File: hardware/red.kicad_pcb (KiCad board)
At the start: 6 copper layers, 40 x 40 mm, 190 parts, among them J1 MICROSDCARD, J2 USB-A, J3 MICRO_HDMI, J4 USB-MINI-B-SMD, J5 STACK-UP-LOW, J6 STACK-DOWN, J7 STACK-UP-LOW, J8 STACK-DOWN, P1 Camera/EXT, Q1 2N7002, Q2 2N7002, Q3 2N7002, SW1 RESET_SW, U1 H5TQ4G63AFR, U2 AXP152, U3 RT9701XB, U4 82400152, U5 TPD4S010DQA, U6 TPD4S010DQA, U7 TPD4S010DQA, U8 82400152, U9 NX3008PBKS, X1 24MHz

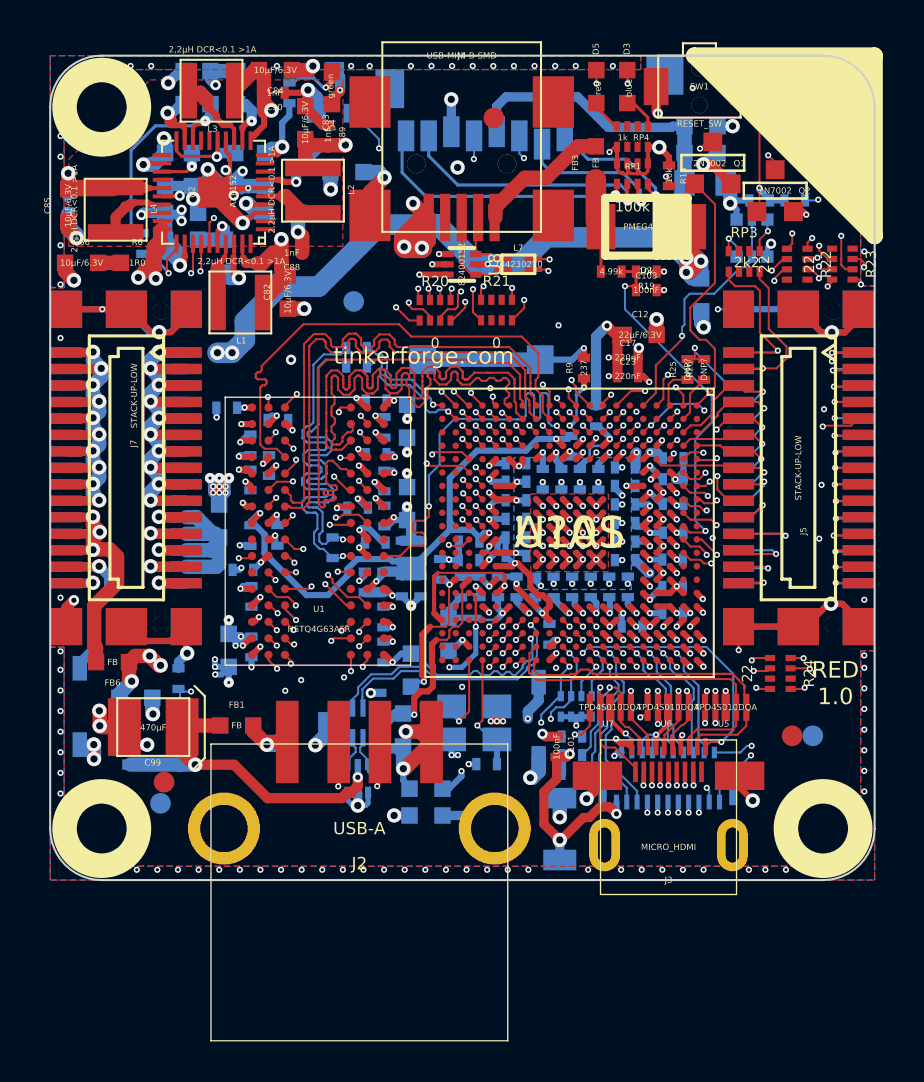
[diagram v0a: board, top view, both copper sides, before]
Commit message: ordered hardware version changed assignment of resistor networks for sdcard signals
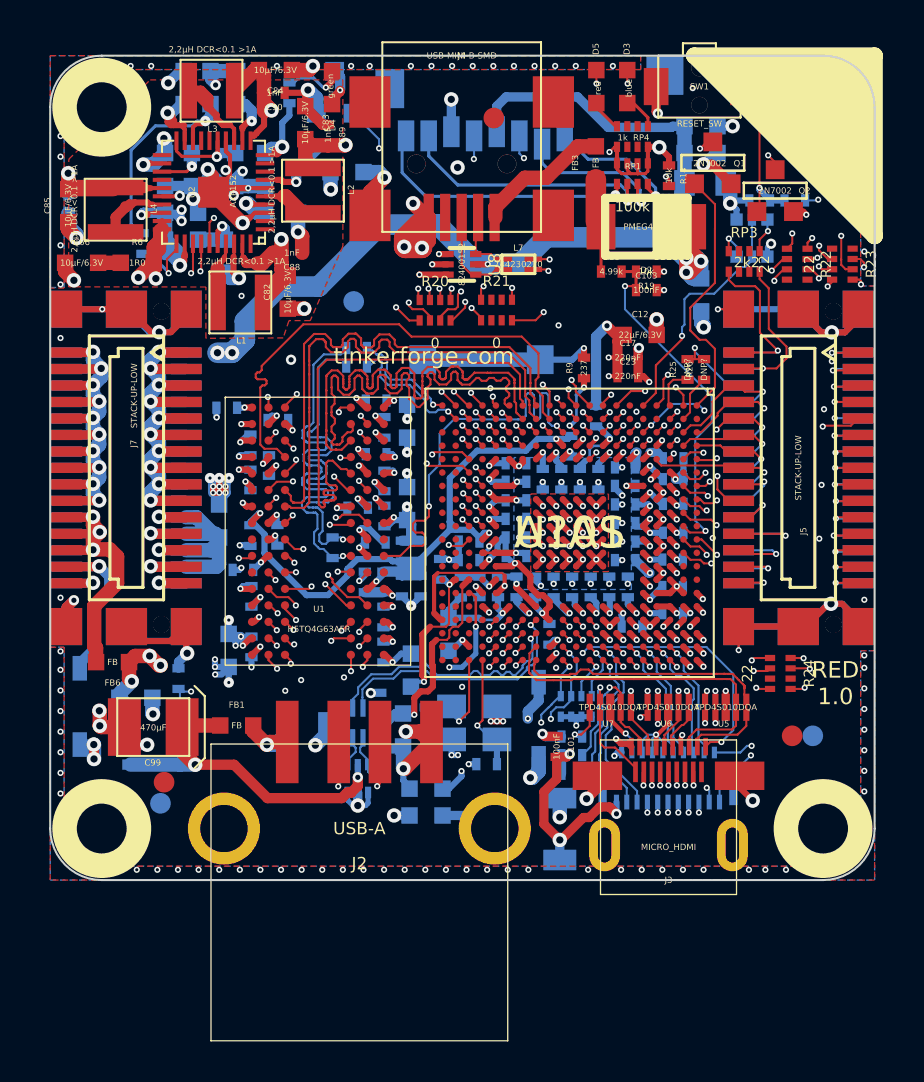
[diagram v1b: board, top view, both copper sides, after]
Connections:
- R20 pad 3: N-00000229 -> N-00000246
- R20 pad 4: N-00000244 -> N-00000243
- R20 pad 5: SDCARD_CMD -> SDCARD_D2
- R20 pad 6: SDCARD_CLK -> SDCARD_D3
- R21 pad 1: N-00000246 -> N-00000244
- R21 pad 4: N-00000243 -> N-00000231
- R21 pad 5: SDCARD_D2 -> SDCARD_CLK
- R21 pad 8: SDCARD_D3 -> SDCARD_CMD
- U?A1 pad K18: N-00000229 -> N-00000231
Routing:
- net N-00000229: track 26.9 -> 0.00 mm, vias 2 -> 0
- net N-00000231: track 0.00 -> 22.1 mm, vias 0 -> 2
- net GND: track 807.3 -> 811.1 mm, vias 313 -> 314
- net SDCARD_D2: track 16.1 -> 19.1 mm
- net N-00000243: track 22.3 -> 25.2 mm
- net SDCARD_D3: track 17.8 -> 19.8 mm
- net SDCARD_CMD: track 17.3 -> 19.1 mm
- net N-00000246: track 27.0 -> 27.9 mm
- net N-00000244: track 24.4 -> 23.5 mm

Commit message: add current hardware version
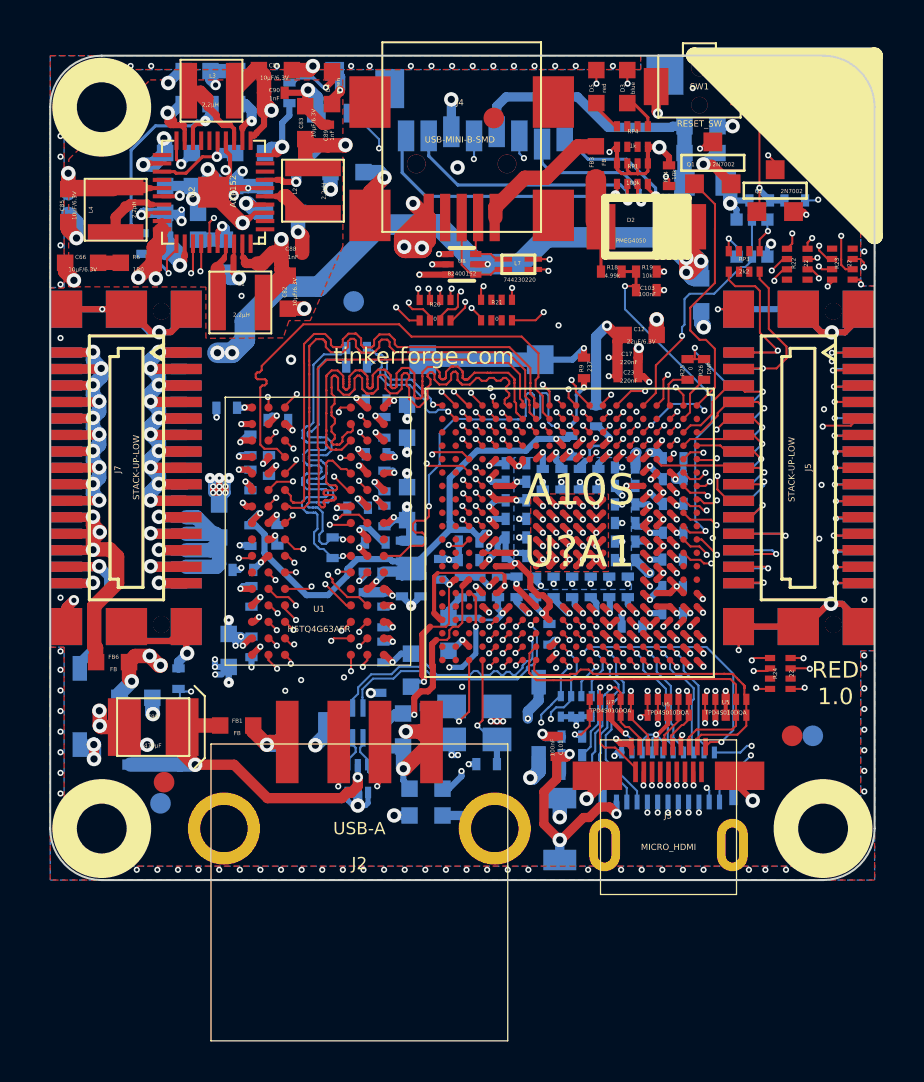
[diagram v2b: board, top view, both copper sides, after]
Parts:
- C100: value TBD -> 100nF
- C15, C3: value TBDpF -> 9pF
- C95: value NA -> DNP
- L1, L2, L3, L4: value 2,2µH DCR<0.1 >1A -> 2,2µH
- R25: value DNP? -> 0
- R26: value DNP? -> DNP
- moved C63 2.10 mm to (134.2, 80.5)
- moved C64 2.10 mm to (136.3, 80.5)
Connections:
- C63 pad 1: N-000007 (its old number) -> N-000008
- C64 pad 1: N-000008 -> N-000009
- U2 pad 15: N-000007 (its old number) -> N-000009
- U2 pad 20: N-000007 (its old number) -> N-000008
- U2 pad 23: N-000008 -> N-000009
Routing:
- net N-000007 (its old number): track 5.10 -> 0.00 mm, vias 1 -> 0
- net N-000009: track 0.00 -> 4.78 mm, vias 0 -> 1
- net LDO0_OUT: track 55.1 -> 53.3 mm

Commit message: * reset button is now used as power button * change reset circuitry:   * stack reset is now connected to interrupt capable GPIO   * RESET_N signal is now used only for internal reset circuitry * fix USB ESD protection ciruitry bug * add inverter for STACK-SER2-RTS signal * UART3_CTS connected to GND * add missing tf logo * change position of different components and labels for easier production
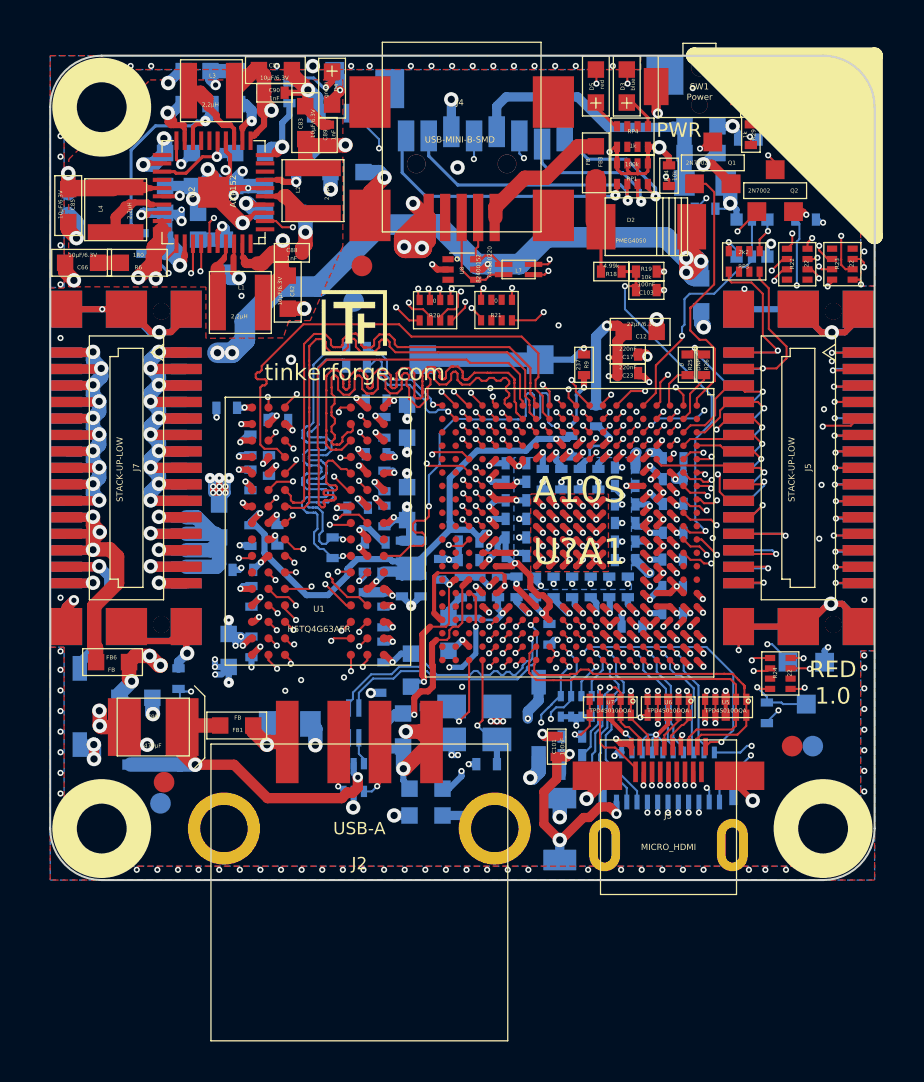
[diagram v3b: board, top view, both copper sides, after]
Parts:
- added C30: 100pF, tinkerforge:0402, B.Cu at (161.2, 79.0)
- added G***: Logo_31x31, logo:Logo_31x31, F.Cu at (140.5, 86.3)
- added Q4: 2N7002, SOT23GDS, B.Cu at (164.0, 105.4)
- added R29: 1k, tinkerforge:0402, F.Cu at (161.3, 78.8)
- added R30: 1k, 0402, B.Cu at (162.1, 106.8)
- C1, C10, C101, C103, C11, C13, C15, C16, C17, C18, C19, C2, C20, C21, C22, C23, C24, C27, C28, C29, C3, C31, C32, C34, C35, C36, C37, C38, C39, C4, C40, C41, C42, C43, C44, C45, C46, C47, C49, C5, C50, C51, C52, C53, C54, C55, C57, C59, C6, C65, C67, C68, C69, C7, C70, C71, C72, C73, C79, C8, C80, C81, C86, C87, C88, C89, C9, C90, C91, C93, C94, C95, R1, R10, R11, R12, R13, R14, R15, R16, R17, R18, R19, R2, R25, R26, R27, R3, R4, R5, R7, R8, R9: footprint 0402 -> tinkerforge:0402
- C100, L5: footprint 0805 -> tinkerforge:0805
- C102, C12, C14, C25, C26, C33, C48, C56, C58, C60, C61, C62, C63, C64, C66, C74, C75, C76, C77, C78, C82, C83, C84, C85, C92, C96, C97, C98, FB1, FB2, FB3, FB4, FB5, FB6, R6: footprint 0603 -> tinkerforge:0603
- C99: footprint 3528-21 -> tinkerforge:3528-21
- D1, D6: footprint SOD-123 -> tinkerforge:SOD-123
- D2: footprint SOD-128 -> tinkerforge:SOD-128
- D3, D4, D5: footprint D0603 -> tinkerforge:D0603
- F1: footprint 1206 -> tinkerforge:1206
- J1: footprint MicroSD_TF001A -> tinkerforge:MicroSD_TF001A
- J2: footprint USB-A-SMT-8231 -> tinkerforge:USB-A-SMT-8231
- J3: footprint MICRO-HDMI-D -> tinkerforge:MICRO-HDMI-D
- J4: footprint USB-MINI-B-SMD -> tinkerforge:USB-MINI-B-SMD
- J5, J7: footprint BTB08-ACS-TOP -> tinkerforge:BTB08-ACS-TOP
- J6, J8: footprint BTB08-ACS-BTM -> tinkerforge:BTB08-ACS-BTM
- L1, L2, L3, L4: footprint NRH3015 -> tinkerforge:NRH3015
- L6, L7: footprint WE-CNSW-0603 -> tinkerforge:WE-CNSW-0603
- P1: footprint 502078-2110-C -> tinkerforge:502078-2110-C
- Q1, Q2, Q3: footprint SOT23GDS -> tinkerforge:SOT23GDS
- R20, R21, R22, R23, R24, RP1, RP2, RP3, RP4: footprint 741X083 -> tinkerforge:741X083
- R28: value 1k -> 100; footprint 0402 -> tinkerforge:0402
- SW1: value RESET_SW -> Power; footprint TACT-SWITCH -> tinkerforge:TACT-SWITCH
- U1: footprint FBGA96 -> tinkerforge:FBGA96
- U2: footprint QFN40_5X5 -> tinkerforge:QFN40_5X5
- U3: footprint SOT23-5 -> tinkerforge:SOT23-5
- U4, U8: footprint SOT563 -> tinkerforge:SOT563
- U5, U6, U7: footprint TPD4S010DQA -> tinkerforge:TPD4S010DQA
- U9: footprint SOT363 -> tinkerforge:SOT363
- U?A1: footprint TFBGA336 -> tinkerforge:TFBGA336
- X1: footprint CRYSTAL_3225 -> tinkerforge:CRYSTAL_3225
- moved Fiducial_Mark 9.61 mm to (142.4, 85.1)
- moved VAL 5.91 mm to (139.1, 88.1)
- moved R3 2.68 mm to (159.1, 82.3), turned to 180 degrees
- moved R28 1.06 mm to (164.0, 82.9)
- moved C100 0.88 mm to (138.9, 107.3)
- moved Fiducial_Mark 0.50 mm to (163.3, 108.4)
- moved Fiducial_Mark 0.50 mm to (164.3, 108.4)
- moved L7 0.25 mm to (150.1, 85.3)
- moved U8 0.25 mm to (147.3, 85.3)
- moved R25 0.23 mm to (158.2, 89.9)
- moved R26 0.23 mm to (159.1, 89.9)
- moved U4 0.21 mm to (142.1, 110.0)
- moved L6 0.20 mm to (142.1, 107.3)
- moved C17 0.15 mm to (155.3, 89.4)
- moved R9 0.15 mm to (153.2, 89.9)
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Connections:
- D3 pad 1: N-00000257 -> Net-(D3-Pad1)
- D3 pad 2: N-00000278 -> Net-(D3-Pad2)
- D4 pad 1: N-00000221 -> Net-(D4-Pad1)
- D4 pad 2: N-00000266 -> Net-(D4-Pad2)
- D5 pad 1: N-00000220 -> Net-(D5-Pad1)
- D5 pad 2: N-00000215 -> Net-(D5-Pad2)
- L6 pad 1: /HDMI/USB/_USB_HOST_UDP1 -> Net-(L6-Pad1)
- L6 pad 4: /HDMI/USB/_USB_HOST_UDM1 -> Net-(L6-Pad4)
- Q1 pad D: N-00000220 -> Net-(D5-Pad2)
- Q2 pad D: N-00000257 -> Net-(D3-Pad2)
- Q3 pad D: N-00000221 -> Net-(D4-Pad2)
- R24 pad 4: N-00000262 -> Net-(Q4-PadD)
- R27 pad 2: N-00000266 -> Net-(D4-Pad1)
- R28 pad 2: RESET_N -> RESET_STACK
- RP4 pad 1: N-00000278 -> Net-(D3-Pad1)
- RP4 pad 4: N-00000215 -> Net-(D5-Pad1)
- SW1 pad 2: RESET_N -> Net-(R29-Pad2)
- U2 pad 2: (no net) -> Net-(C30-Pad2)
- U4 pad 1: GND -> /HDMI/USB/_USB_HOST_UDP1
- U4 pad 3: GND -> /HDMI/USB/_USB_HOST_UDM1
- U4 pad 4: /HDMI/USB/_USB_HOST_UDM1 -> Net-(L6-Pad4)
- U4 pad 6: /HDMI/USB/_USB_HOST_UDP1 -> Net-(L6-Pad1)
- U8 pad 1: GND -> (no net)
- U8 pad 3: GND -> (no net)
- U?A1 pad A6: (no net) -> GND
- U?A1 pad B7: N-00000262 -> Net-(Q4-PadG)
- U?A1 pad D2: (no net) -> RESET_STACK
- U?A1 pad M19: GND -> +3.3V
- U?A1 pad M20: GND -> +3.3V
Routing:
- net Net-(C30-Pad2): track 0.00 -> 29.5 mm, vias 0 -> 2
- net RESET_STACK: track 0.00 -> 13.1 mm, vias 0 -> 2
- net N-00000262: track 13.1 -> 0.00 mm, vias 2 -> 0
- net Net-(Q4-PadG): track 0.00 -> 11.6 mm, vias 0 -> 2
- net Net-(D3-Pad2): track 0.00 -> 9.77 mm, vias 0 -> 2
- net N-00000257: track 9.77 -> 0.00 mm, vias 2 -> 0
- net Net-(D5-Pad2): track 0.00 -> 9.48 mm, vias 0 -> 2
- net N-00000220: track 9.48 -> 0.00 mm, vias 2 -> 0
- net RESET_N: track 64.3 -> 57.4 mm, vias 3 -> 4
- net GND: track 811.1 -> 816.8 mm, vias 314 -> 313
- net Net-(Q4-PadD): track 0.00 -> 3.54 mm, vias 0 -> 1
- net Net-(D4-Pad1): track 0.00 -> 2.97 mm, vias 0 -> 1
- net N-00000266: track 2.97 -> 0.00 mm, vias 1 -> 0
- net Net-(R29-Pad2): track 0.00 -> 2.00 mm
- net /HDMI/USB/_USB_HOST_UDP1: track 4.94 -> 2.95 mm
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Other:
- board text added: "PWR"

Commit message: change wrong component silkscreen outlines
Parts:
- Q4: footprint SOT23GDS -> tinkerforge:SOT23GDS
- R30: footprint 0402 -> tinkerforge:0402

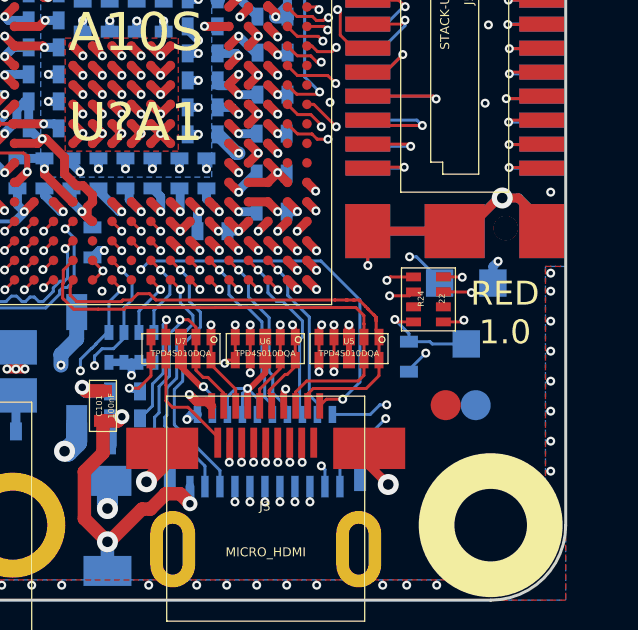
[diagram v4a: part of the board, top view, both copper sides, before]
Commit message: remove inverter for rts
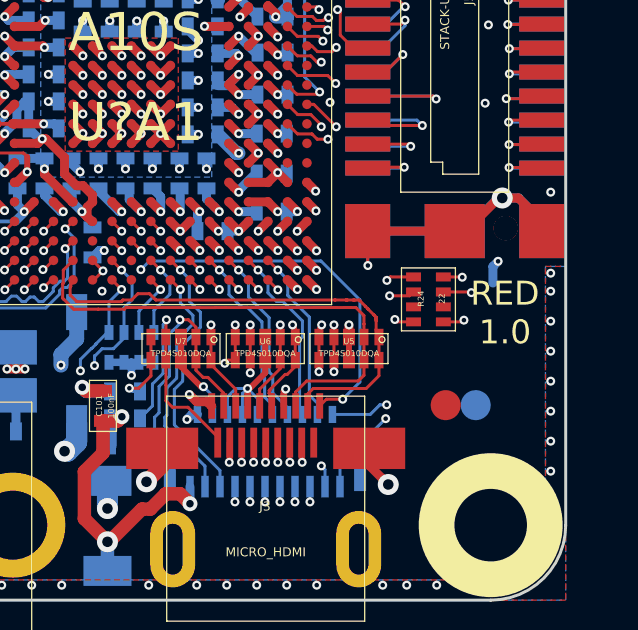
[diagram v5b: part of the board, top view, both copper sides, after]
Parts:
- removed Q4: 2N7002, tinkerforge:SOT23GDS
- removed R30: 1k, tinkerforge:0402
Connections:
- R24 pad 4: Net-(Q4-PadD) -> Net-(R24-Pad4)
- U?A1 pad B7: Net-(Q4-PadG) -> Net-(R24-Pad4)
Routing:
- net Net-(R24-Pad4): track 0.00 -> 13.0 mm, vias 0 -> 2
- net Net-(Q4-PadG): track 11.6 -> 0.00 mm, vias 2 -> 0
- net Net-(Q4-PadD): track 3.54 -> 0.00 mm, vias 1 -> 0
- net +3.3V: track 193.2 -> 192.3 mm, vias 22 -> 21
